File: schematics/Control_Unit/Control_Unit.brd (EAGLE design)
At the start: 49.8 x 49.8 mm, 222 parts, among them IC1 74HCT32N, IC10 74HC74N, IC100 74HCT374N, IC101 74HCT08N, IC102 74HC151N, IC103 74HC373N, IC105 74HC151N, IC106 74HC151N, IC108 74HCT32N, IC11 74HC74N, IC110 74HCT32N, IC111 74HC151N, IC112 74HCT32N, IC113 74HC151N, IC114 74HC151N, IC115 74HC151N, IC116 74HC373N, IC12 74AC08N, IC124 74HCT32N, IC125 74HCT08N, IC126 74AC157N, IC127 74HCT08N, IC128 74AC08N, IC129 74AC08N, IC13 74AC08N, IC135 74HCT08N, IC136 74HCT08N, IC14 74HC74N, IC141 74HCT32N, IC15 74HC74N, IC16 74AC08N, IC168 74HCT32N, IC17 74HCT32N, IC173 74HCT32N, IC175 74HC193N, IC176 74HC193N, IC177 74HC193N, IC178 74HC193N, IC179 74HC193N, IC18 74AC08N, IC180 74HC193N, IC181 74HC193N, IC182 74HC193N, IC19 74AC08N, IC191 74HCT32N, IC2 74HCT32N, IC20 74AC08N, IC21 74AC08N, IC22 74HCT32N, IC23 74HCT08N, IC24 74HCT08N, IC25 74HCT32N, IC26 74HCT08N, IC27 74HCT08N, IC28 74HCT08N, IC3 74HC151N, IC30 74HCT08N, IC31 74HCT00N, IC34 74HCT08N, IC35 74HCT04N, IC36 74HCT32N, IC39 74HCT08N, IC4 74AC08N, IC41 74HCT08N, IC42 74HC373N, IC43 74HCT04N, IC44 74ACT157N, IC46 74ACT157N, IC47 74HCT04N, IC48 74ACT02N, IC49 74AC86N, IC5 74ACT02N, IC51 74HCT08N, IC52 74HCT32N, IC55 74HCT32N, IC56 74HC151N, IC57 74HC151N, IC58 74HC151N, IC59 74HC151N, IC6 74HC193N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

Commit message: renumber schematic parts
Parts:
- removed C117, C120, C121, C122, C123, C127, C142, C143, C145, C148, C150, C151, C154: (no value), rcl:C1206
- removed IC110, IC112, IC124, IC168, IC173, IC191: 74HCT32N, 74xx-eu:DIL14
- removed IC113, IC114, IC115: 74HC151N, 74xx-eu:DIL16
- removed IC116: 74HC373N, 74xx-eu:DIL20
- removed IC125, IC127, IC135, IC136: 74HCT08N, 74xx-eu:DIL14
- removed IC126: 74AC157N, 74xx-eu:DIL16
- removed IC128, IC129: 74AC08N, 74xx-eu:DIL14
- removed IC175, IC176, IC177, IC179, IC180, IC181, IC182: 74HC193N, custom_parts:DIL16
- removed JP10: (no value), pinhead:2X20
- added C108, C24, C25, C37, C41, C45, C46, C54, C62, C66, C69, C76, C81: (no value), rcl:C1206
- added IC104: 74ACT157N, 74xx-eu:DIL16
- added IC107, IC62, IC76, IC92: 74HCT08N, 74xx-eu:DIL14
- added IC109: 74HCT00N, 74xx-eu:DIL14
- added IC29: 74ACT02N, 74xx-eu:DIL14
- added IC33, IC45, IC66, IC81: 74HCT374N, 74xx-eu:DIL20
- added IC37, IC38, IC50: 74HC151N, 74xx-eu:DIL16
- added IC40, IC68, IC94, IC96: 74HCT32N, 74xx-eu:DIL14
- added IC53, IC54: 74HC74N, 74xx-eu:DIL14
- added IC67: 74HCT04N, 74xx-eu:DIL14
- added IC69, IC75: 74HC193N, custom_parts:DIL16
- added IC95: 74AC08N, 74xx-eu:DIL14
- added JP4: (no value), pinhead:2X20
- IC10: value 74HC74N -> 74HCT08N
- IC100, IC99: value 74HCT374N -> 74HCT08N; device 74xx-eu:DIL20 -> 74xx-eu:DIL14
- IC101: value 74HCT08N -> 74HC373N; device 74xx-eu:DIL14 -> 74xx-eu:DIL20
- IC102, IC106, IC57, IC58, IC60: value 74HC151N -> 74HC193N; device 74xx-eu:DIL16 -> custom_parts:DIL16
- IC105, IC56, IC61: value 74HC151N -> 74HCT32N; device 74xx-eu:DIL16 -> 74xx-eu:DIL14
- IC108, IC2: value 74HCT32N -> 74HCT08N
- IC11: value 74HC74N -> 74ACT157N; device 74xx-eu:DIL14 -> 74xx-eu:DIL16
- IC12, IC13, IC21: value 74AC08N -> 74ACT157N; device 74xx-eu:DIL14 -> 74xx-eu:DIL16
- IC14: value 74HC74N -> 74HCT04N
- IC15: value 74HC74N -> 74HC151N; device 74xx-eu:DIL14 -> 74xx-eu:DIL16
- IC16, IC4: value 74AC08N -> 74HC151N; device 74xx-eu:DIL14 -> 74xx-eu:DIL16
- IC18: value 74AC08N -> 74HCT374N; device 74xx-eu:DIL14 -> 74xx-eu:DIL20
- IC19: value 74AC08N -> 74ACT02N
- IC20: value 74AC08N -> 74HCT08N
- IC22: value 74HCT32N -> 74HC151N; device 74xx-eu:DIL14 -> 74xx-eu:DIL16
- IC23, IC51: value 74HCT08N -> 74HC151N; device 74xx-eu:DIL14 -> 74xx-eu:DIL16
- IC25: value 74HCT32N -> 74AC86N
- IC26, IC41: value 74HCT08N -> 74HCT374N; device 74xx-eu:DIL14 -> 74xx-eu:DIL20
- IC27, IC34: value 74HCT08N -> 74ACT157N; device 74xx-eu:DIL14 -> 74xx-eu:DIL16
- IC28: value 74HCT08N -> 74AC08N
- IC31: value 74HCT00N -> 74HC151N; device 74xx-eu:DIL14 -> 74xx-eu:DIL16
- IC35: value 74HCT04N -> 74HC373N; device 74xx-eu:DIL14 -> 74xx-eu:DIL20
- IC36: value 74HCT32N -> 74HC373N; device 74xx-eu:DIL14 -> 74xx-eu:DIL20
- IC39: value 74HCT08N -> 74ACT02N
- IC42: value 74HC373N -> 74HC151N; device 74xx-eu:DIL20 -> 74xx-eu:DIL16
- IC43, IC47: value 74HCT04N -> 74HC151N; device 74xx-eu:DIL14 -> 74xx-eu:DIL16
- IC44: value 74ACT157N -> 74ACT02N; device 74xx-eu:DIL16 -> 74xx-eu:DIL14
- IC46: value 74ACT157N -> 74HC151N
- IC48, IC8: value 74ACT02N -> 74HCT32N
- IC49: value 74AC86N -> 74HCT32N
- IC5, IC85: value 74ACT02N -> 74HCT374N; device 74xx-eu:DIL14 -> 74xx-eu:DIL20
- IC52, IC55: value 74HCT32N -> 74HC74N
- IC59: value 74HC151N -> 74HCT08N; device 74xx-eu:DIL16 -> 74xx-eu:DIL14
- IC6, IC7, IC82, IC83: value 74HC193N -> 74AC08N; device custom_parts:DIL16 -> 74xx-eu:DIL14
- IC63, IC70, IC71, IC84: value 74HCT374N -> 74HCT32N; device 74xx-eu:DIL20 -> 74xx-eu:DIL14
- IC64, IC93: value 74HCT374N -> 74HC193N; device 74xx-eu:DIL20 -> custom_parts:DIL16
- IC72: value 74HC373N -> 74HCT08N; device 74xx-eu:DIL20 -> 74xx-eu:DIL14
- IC74: value 74HCT08N -> 74HC193N; device 74xx-eu:DIL14 -> custom_parts:DIL16
- IC77, IC87: value 74ACT157N -> 74AC08N; device 74xx-eu:DIL16 -> 74xx-eu:DIL14
- IC79: value 74ACT157N -> 74HCT374N; device 74xx-eu:DIL16 -> 74xx-eu:DIL20
- IC80: value 74HCT32N -> 74HC193N; device 74xx-eu:DIL14 -> custom_parts:DIL16
- IC86: value 74ACT157N -> 74HCT04N; device 74xx-eu:DIL16 -> 74xx-eu:DIL14
- IC88, IC89: value 74ACT157N -> 74HCT08N; device 74xx-eu:DIL16 -> 74xx-eu:DIL14
- IC9: value 74HC151N -> 74AC157N
- IC90, IC91: value 74HCT374N -> 74AC08N; device 74xx-eu:DIL20 -> 74xx-eu:DIL14
- IC98: value 74HC151N -> 74ACT157N
- JP1: device pinhead:2X20 -> pinhead:2X15
- JP3: device pinhead:2X15 -> pinhead:2X20
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- renumbered C110 to C107, C111 to C106, C112 to C103, C113 to C105, C114 to C104, C116 to C102, C118 to C101, C126 to C98, C129 to C100, C130 to C95, C131 to C97, C132 to C96, C141 to C94, C144 to C92, C146 to C89, C147 to C88, C153 to C83, IC111 to IC32, IC141 to IC65, IC178 to IC97, JP9 to JP5
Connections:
- net !CLR_CARRY_BIT: now also IC55.13, JP4.12; no longer IC15.13, JP1.12
- net !IR_DATA_OUT_7: now also IC40.12, IC59.10, IC86.10, IC88.12; no longer IC101.12, IC127.10, IC36.12, IC47.10
- net !OPCODE_5: now also IC14.6, IC28.2, IC28.5, IC92.10; no longer IC129.2, IC129.5, IC26.10, IC43.6
- net !REGISTER_RESET: now also IC102.14, IC106.14, IC57.14, IC58.14, IC60.14, IC64.14, IC69.14, IC74.14, IC75.14, IC80.14, IC93.14, JP4.8; no longer IC175.14, IC176.14, IC177.14, IC179.14, IC180.14, IC181.14, IC182.14, IC6.14, IC7.14, IC82.14, IC83.14, JP1.8
- net !RING_CNTR_RESET: now also IC52.13, IC52.4, IC53.1, IC53.13, IC54.1, IC54.13, IC55.1, JP4.10; no longer IC10.13, IC10.4, IC11.1, IC11.13, IC14.1, IC14.13, IC15.1, JP1.10
- net !SET_CARRY_BIT: now also IC55.10, JP4.14; no longer IC15.10, JP1.14
- net !TWO_BYTE_CMD: now also IC14.11, IC89.10, IC96.8; no longer IC108.8, IC23.10, IC43.11
- net ADRR_0: now also IC13.4, JP1.1; no longer IC86.4, JP2.1
- net ADRR_1: now also IC13.7, JP1.3; no longer IC86.7, JP2.3
- net ADRR_10: now also IC27.9, JP1.21; no longer IC88.9, JP2.21
- net ADRR_11: now also IC27.12, JP1.23; no longer IC88.12, JP2.23
- net ADRR_12: now also IC34.4, JP1.25; no longer IC89.4, JP2.25
- net ADRR_13: now also IC34.7, JP1.27; no longer IC89.7, JP2.27
- net ADRR_14: now also IC34.9, JP1.29; no longer IC89.9, JP2.29
- net ADRR_15: now also IC34.12, IC67.5, IC68.9; no longer IC17.9, IC35.5, IC89.12
- net ADRR_2: now also IC13.9, JP1.5; no longer IC86.9, JP2.5
- net ADRR_3: now also IC13.12, JP1.7; no longer IC86.12, JP2.7
- net ADRR_4: now also IC21.4, JP1.9; no longer IC87.4, JP2.9
- net ADRR_5: now also IC21.7, JP1.11; no longer IC87.7, JP2.11
- net ADRR_6: now also IC21.9, JP1.13; no longer IC87.9, JP2.13
- net ADRR_7: now also IC21.12, JP1.15; no longer IC87.12, JP2.15
- net ADRR_8: now also IC27.4, JP1.17; no longer IC88.4, JP2.17
- net ADRR_9: now also IC27.7, JP1.19; no longer IC88.7, JP2.19
- net ALU_CARRY_BIT: now also IC55.9, IC62.4, JP4.16; no longer IC15.9, IC34.4, JP1.16
- net ALU_CARRY_IN: now also IC62.6; no longer IC34.6
- net ALU_CARRY_OUT: now also IC109.12, IC55.12, IC88.9; no longer IC101.9, IC15.12, IC31.12
- net ALU_NR1_ENABLE_ALU: now also IC49.9, IC70.1, IC77.3; no longer IC18.3, IC191.1, IC25.9
- net ALU_NR1_ENABLE_JMP_O_PTR_ADD: now also IC49.10, IC59.8; no longer IC127.8, IC25.10
- net ALU_NR2_ENABLE_ALU: now also IC49.12, IC70.2, IC77.6; no longer IC18.6, IC191.2, IC25.12
- net ALU_NR2_ENABLE_JMP_O_PTR_ADD: now also IC108.8, IC49.13; no longer IC125.8, IC25.13
- net ALU_NR3_ENABLE_ALU: now also IC70.4, IC77.8; no longer IC18.8, IC191.4
- net ALU_NR4_ENABLE_ALU: now also IC70.5, IC77.11; no longer IC18.11, IC191.5
- net CLR_NOT_CS/FILL_REGISTER_LDR: now also IC105.1, IC107.8, IC68.4, IC96.5; no longer IC108.5, IC17.4, IC173.1, IC27.8
- net CLR_NOT_CS_POP/FILL_REGISTER_POP: now also IC108.3, IC19.9, IC39.11, IC96.4; no longer IC108.4, IC125.3, IC48.11, IC85.9
- net CLR_NOT_CS_PUSH: now also IC105.4, IC107.3, IC19.8; no longer IC173.4, IC27.3, IC85.8
- net CLR_NOT_CS_STR: now also IC105.9, IC107.11, IC68.2; no longer IC17.2, IC173.9, IC27.11
- net CLR_NOT_OE/CLR_NOT_CS_CYCL_1/2: now also IC19.11, IC68.1, IC84.6; no longer IC17.1, IC80.6, IC85.11
- net CLR_NOT_OE/CLR_NOT_CS_CYCL_3/4: now also IC68.5, IC84.11; no longer IC17.5, IC80.11
- net CLR_NOT_OE_POP: now also IC39.13, JP2.4; no longer IC48.13, JP3.4
- net CNNCT_PTR_TO_ABUS/CNNCT_REG_TO_DBUS/CLR_NOT_WE/SEL_2_STR: now also IC105.8, IC17.9, IC40.2, IC67.3; no longer IC173.8, IC2.9, IC35.3, IC36.2
- net CONNECT_PTR_TO_ABUS/CLR_NOT_OE_LDR: now also IC105.3, IC19.12, IC40.1; no longer IC173.3, IC36.1, IC85.12
- net CONNECT_REG_TO_DBUS/CLR_NOT_WE/SELECTOR_TABLE_2_PUSH: now also IC105.6, IC17.10, IC67.1; no longer IC173.6, IC2.10, IC35.1
- net CONNECT_REG_TO_DBUS_PTR/FILL_PTR_L_SET_PTR: now also IC39.3, IC61.4, IC99.11; no longer IC24.11, IC48.3, IC52.4
- net CYCL_1: now also IC52.12, IC52.5, IC84.5, JP4.22; no longer IC10.12, IC10.5, IC80.5, JP1.22
- net DATA0: now also IC101.2, IC18.3, IC26.3, IC33.3, IC35.2, IC36.2, IC41.3, IC45.3, IC5.3, IC57.15, IC60.15, IC66.3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; no longer IC100.3, IC116.2, IC179.15, IC181.15, IC42.2, IC63.3, IC64.3, IC70.3, IC71.3, IC72.2, IC77.2, IC82.15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
- net DATA1: now also IC101.5, IC18.4, IC26.4, IC33.4, IC35.5, IC36.5, IC41.4, IC45.4, IC5.4, IC57.1, IC60.1, IC66.4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; no longer IC100.4, IC116.5, IC179.1, IC181.1, IC42.5, IC63.4, IC64.4, IC70.4, IC71.4, IC72.5, IC77.5, IC82.1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
- net DATA2: now also IC101.6, IC18.7, IC26.7, IC33.7, IC35.6, IC36.6, IC41.7, IC45.7, IC5.7, IC57.10, IC60.10, IC66.7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; no longer IC100.7, IC116.6, IC179.10, IC181.10, IC42.6, IC63.7, IC64.7, IC70.7, IC71.7, IC72.6, IC77.11, IC82.10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
- net DATA3: now also IC101.9, IC18.8, IC26.8, IC33.8, IC35.9, IC36.9, IC41.8, IC45.8, IC5.8, IC57.9, IC60.9, IC66.8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; no longer IC100.8, IC116.9, IC179.9, IC181.9, IC42.9, IC63.8, IC64.8, IC70.8, IC71.8, IC72.9, IC77.14, IC82.9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
- net DATA4: now also IC101.12, IC104.2, IC18.13, IC26.13, IC33.13, IC35.12, IC36.12, IC41.13, IC45.13, IC5.13, IC58.15, IC64.15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; no longer IC100.13, IC116.12, IC180.15, IC182.15, IC42.12, IC63.13, IC64.13, IC70.13, IC71.13, IC72.12, IC79.2, IC83.15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
- net DATA5: now also IC101.15, IC104.5, IC18.14, IC26.14, IC33.14, IC35.15, IC36.15, IC41.14, IC45.14, IC5.14, IC58.1, IC64.1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; no longer IC100.14, IC116.15, IC180.1, IC182.1, IC42.15, IC63.14, IC70.14, IC71.14, IC72.15, IC79.5, IC83.1, IC84.14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
- net DATA6: now also IC101.16, IC104.11, IC18.17, IC26.17, IC33.17, IC35.16, IC36.16, IC41.17, IC45.17, IC5.17, IC58.10, IC64.10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; no longer IC100.17, IC116.16, IC180.10, IC182.10, IC42.16, IC63.17, IC64.14, IC64.17, IC70.17, IC71.17, IC72.16, IC79.11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
- net DATA7: now also IC101.19, IC104.14, IC18.18, IC26.18, IC33.18, IC35.19, IC36.19, IC41.18, IC45.18, IC5.18, IC58.9, IC64.9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; no longer IC100.18, IC116.19, IC180.9, IC182.9, IC42.19, IC63.18, IC64.18, IC70.18, IC71.18, IC72.19, IC79.14, IC83.9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
- net DATA_BUS_ENABLE_LATCH: now also IC35.11, IC59.3, IC67.9; no longer IC127.3, IC35.9, IC72.11
- net DBUS_SELECTOR_TABLE_2: now also IC11.1, IC17.8, IC63.1; no longer IC110.1, IC2.8, IC46.1
- net FDSGDFGFDSGFSDGFDGSDG: now also IC19.1, IC8.10, IC8.13; no longer IC22.10, IC22.13, IC85.1
- net FSDFAFSDFSFDDDDDDDDDDDDDDDDDDDDDDDDDDDDDDDD1: now also IC10.10, IC10.2, IC2.10, IC2.2, IC20.6; no longer IC136.6, IC39.10, IC39.2, IC41.10, IC41.2
- net GND: now also C108.2, C24.2, C25.2, C37.2, C41.2, C45.2, C46.2, C54.2, C62.2, C66.2, C69.2, C76.2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; no longer C117.2, C120.2, C121.2, C122.2, C123.2, C127.2, C142.2, C143.2, C145.2, C148.2, C150.2, C151.2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
- net HGGJHGGJZGZ77UZGHGHHGHGHGHGHJGHJ: now also IC100.8, IC105.2; no longer IC173.2, IC51.8
- net INPUT_REG0/OPC4/5_IS_NULL: now also IC109.5, IC2.1, IC2.4, IC24.1, IC24.4, IC28.3, IC88.1, IC9.3; no longer IC101.1, IC126.3, IC129.3, IC135.1, IC135.4, IC31.5, IC41.1, IC41.4
- net INPUT_REG1: now also IC2.12, IC2.9, IC24.12, IC24.9, IC28.6, IC9.6; no longer IC126.6, IC129.6, IC135.12, IC135.9, IC41.12, IC41.9
- net INPUT_REG2: now also IC10.1, IC10.4, IC28.8, IC9.10; no longer IC126.10, IC129.8, IC39.1, IC39.4
- net INPUT_REG3: now also IC10.12, IC10.9, IC28.11, IC9.13; no longer IC126.13, IC129.11, IC39.12, IC39.9
- net INPUT_REG_IS_NOT_OUTPUT_REG: now also IC17.6, IC19.3, IC6.1, IC6.12, IC6.4, IC6.9, IC96.9; no longer IC108.9, IC2.6, IC4.1, IC4.12, IC4.4, IC4.9, IC85.3
- net IO_INPUT1_0: now also IC3.12, JP3.2; no longer IC61.12, JP10.2
- net IO_INPUT1_1: now also IC15.12, JP3.4; no longer IC60.12, JP10.4
- net IO_INPUT1_2: now also IC22.12, JP3.6; no longer IC59.12, JP10.6
- net IO_INPUT1_3: now also IC31.12, JP3.8; no longer IC58.12, JP10.8
- net IO_INPUT1_4: now also IC37.12, JP3.10; no longer IC57.12, JP10.10
- net IO_INPUT1_5: now also IC42.12, JP3.12; no longer IC56.12, JP10.12
- net IO_INPUT1_6: now also IC46.12, JP3.14; no longer IC3.12, JP10.14
- net IO_INPUT1_7: now also IC50.12, JP3.16; no longer IC9.12, JP10.16
- net IO_INPUT2_0: now also IC4.15, JP3.24; no longer IC115.15, JP10.24
- net IO_INPUT2_1: now also IC16.15, JP3.26; no longer IC114.15, JP10.26
- net IO_INPUT2_2: now also IC23.15, JP3.28; no longer IC113.15, JP10.28
- net IO_INPUT2_3: now also JP3.30; no longer JP10.30
- net IO_INPUT2_4: now also IC38.15, JP3.32; no longer IC106.15, JP10.32
- net IO_INPUT2_5: now also IC43.15, JP3.34; no longer IC105.15, JP10.34
- net IO_INPUT2_6: now also IC47.15, JP3.36; no longer IC98.15, JP10.36
- net IO_INPUT2_7: now also IC51.15, JP3.38; no longer IC102.15, JP10.38
- net IO_OUTPUT1_0: now also IC4.14, IC73.2, JP3.1; no longer IC115.14, IC63.2, JP10.1
- net IO_OUTPUT1_1: now also IC16.14, IC73.5, JP3.3; no longer IC114.14, IC63.5, JP10.3
- net IO_OUTPUT1_2: now also IC23.14, IC73.6, JP3.5; no longer IC113.14, IC63.6, JP10.5
- net IO_OUTPUT1_3: now also IC73.9, JP3.7; no longer IC63.9, JP10.7
- net IO_OUTPUT1_4: now also IC38.14, IC73.12, JP3.9; no longer IC106.14, IC63.12, JP10.9
- net IO_OUTPUT1_5: now also IC43.14, IC73.15, JP3.11; no longer IC105.14, IC63.15, JP10.11
- net IO_OUTPUT1_6: now also IC47.14, IC73.16, JP3.13; no longer IC63.16, IC98.14, JP10.13
- net IO_OUTPUT1_7: now also IC51.14, IC73.19, JP3.15; no longer IC102.14, IC63.19, JP10.15
- net IO_OUTPUT2_0: now also IC4.13, IC79.2, JP3.23; no longer IC115.13, IC64.2, JP10.23
- net IO_OUTPUT2_1: now also IC16.13, IC79.5, JP3.25; no longer IC114.13, IC64.5, JP10.25
- net IO_OUTPUT2_2: now also IC23.13, IC79.6, JP3.27; no longer IC113.13, IC64.6, JP10.27
- net IO_OUTPUT2_3: now also IC79.9, JP3.29; no longer IC64.9, JP10.29
- net IO_OUTPUT2_4: now also IC38.13, IC79.12, JP3.31; no longer IC106.13, IC64.12, JP10.31
- net IO_OUTPUT2_5: now also IC43.13, IC79.15, JP3.33; no longer IC105.13, IC64.15, JP10.33
- net IO_OUTPUT2_6: now also IC47.13, IC79.16, JP3.35; no longer IC64.16, IC98.13, JP10.35
- net IO_OUTPUT2_7: now also IC51.13, IC79.19, JP3.37; no longer IC102.13, IC64.19, JP10.37
- net IO_OUTPUT_REG_1_LOAD_INPUT: now also IC10.8, IC73.11; no longer IC39.8, IC63.11
- net IO_OUTPUT_REG_2_LOAD_INPUT: now also IC10.11, IC79.11; no longer IC39.11, IC64.11
- net IR_DATA_OUT_0: now also IC3.4, IC41.2; no longer IC61.4, IC90.2
- net IR_DATA_OUT_1: now also IC15.4, IC41.5; no longer IC60.4, IC90.5
- net IR_DATA_OUT_2: now also IC22.4, IC41.6; no longer IC59.4, IC90.6
- net IR_DATA_OUT_3: now also IC31.4, IC41.9; no longer IC58.4, IC90.9
- net IR_DATA_OUT_4: now also IC37.4, IC41.12; no longer IC57.4, IC90.12
- net IR_DATA_OUT_5: now also IC41.15, IC42.4; no longer IC56.4, IC90.15
- net IR_DATA_OUT_6: now also IC41.16, IC46.4; no longer IC3.4, IC90.16
- net IR_DATA_OUT_7: now also IC108.10, IC40.9, IC41.19, IC50.4, IC86.11, IC88.4; no longer IC101.4, IC125.10, IC36.9, IC47.11, IC9.4, IC90.19
- net IR_LOAD_INPUT/PC_COUNT_UP_FETCH2/CYCL_4: now also IC41.11, IC49.1, IC53.9, IC56.2, IC84.12, JP4.28; no longer IC1.2, IC11.9, IC25.1, IC80.12, IC90.11, JP1.28
- net LATCH_ALU_INPUT_B_ALU: now also IC63.12, IC71.1, IC72.3; no longer IC110.12, IC124.1, IC28.3
- net LATCH_ALU_INPUT_B_JMP_O: now also IC63.9, IC84.1; no longer IC110.9, IC80.1
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
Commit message: fix WRITE_TO_DBUS signal
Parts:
- removed IC62: 74HCT08N, 74xx-eu:DIL14
- added IC112: 74HCT32N, 74xx-eu:DIL14
- added IC118, IC131: 74HC74N, 74xx-eu:DIL14
- added IC126, IC130: 74HCT08N, 74xx-eu:DIL14
- IC105: value 74HCT32N -> 74HC74N
- IC129: value 74HCT32N -> 74HCT04N
- IC52: value 74HC74N -> 74HCT08N
- IC55: value 74HC74N -> 74HCT32N
- moved IC55 52.7 mm to (61.9, 31.1)
- moved IC105 44.8 mm to (30.5, 44.8)
- moved IC52 27.0 mm to (3.17, 9.21)
- renumbered IC107 to IC125, IC63 to IC129
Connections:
- net N$32 renamed REG_TO_DBUS_L_JMP_RET
- net N$33 renamed REG_TO_DBUS_H_JMP_RET
- removed net CLR_NOT_CS/FILL_REGISTER_LDR: IC105.1, IC125.8, IC68.4, IC96.5
- removed net CLR_NOT_CS_POP/FILL_REGISTER_POP: IC108.3, IC19.9, IC39.11, IC96.4
- removed net CLR_NOT_CS_PUSH: IC105.4, IC125.3, IC19.8
- removed net CLR_NOT_CS_STR: IC105.9, IC125.11, IC68.2
- removed net CLR_NOT_OE/CLR_NOT_CS_CYCL_1/2: IC19.11, IC68.1, IC84.6
- removed net CLR_NOT_OE/CLR_NOT_CS_CYCL_3/4: IC68.5, IC84.11
- removed net CLR_NOT_OE_POP: IC39.13, JP2.4
- removed net CNNCT_PTR_TO_ABUS/CNNCT_REG_TO_DBUS/CLR_NOT_WE/SEL_2_STR: IC105.8, IC17.9, IC40.2, IC67.3
- removed net CONNECT_PTR_TO_ABUS/CLR_NOT_OE_LDR: IC105.3, IC19.12, IC40.1
- removed net CONNECT_REG_TO_DBUS/CLR_NOT_WE/SELECTOR_TABLE_2_PUSH: IC105.6, IC17.10, IC67.1
- removed net CONNECT_REG_TO_DBUS_PTR/FILL_PTR_L_SET_PTR: IC39.3, IC61.4, IC99.11
- removed net CYCL_1: IC52.12, IC52.5, IC84.5, JP4.22
- removed net HGGJHGGJZGZ77UZGHGHHGHGHGHGHJGHJ: IC100.8, IC105.2
- removed net IR_LOAD_INPUT/PC_COUNT_UP_FETCH2/CYCL_4: IC41.11, IC49.1, IC53.9, IC56.2, IC84.12, JP4.28
- removed net LATCH_ALU_INPUT_B_ALU: IC129.12, IC71.1, IC72.3
- removed net LATCH_ALU_INPUT_B_JMP_O: IC129.9, IC78.11, IC84.1
- removed net LATCH_ALU_INPUT_B_PTR_ADD: IC105.12, IC129.10, IC89.3
- removed net N$109: IC76.11, IC84.2
- removed net N$110: IC71.2, IC76.6
- removed net N$123: IC100.11, IC105.10
- removed net N$132: IC108.6, IC71.4, IC72.13, IC76.13, IC78.13
- removed net N$146: IC105.5, IC125.6
- removed net N$151: IC105.13, IC99.6
- removed net N$152: IC129.13, IC129.8
- removed net N$157: IC100.6, IC39.12
- removed net OPCODE_LOAD_INPUT/CYCL_2: IC45.11, IC52.9, IC53.2, IC84.4, JP4.24
- removed net PC_COUNT_UP_FETCH1/CYCL_3: IC53.12, IC56.1, IC84.13, IC89.11, JP4.26
- removed net PTR_ADD_OR_JMP_O_OR_ALU_FILL: IC1.4, IC1.8, IC14.9
- removed net STATE_0/CYCL_5: IC100.12, IC100.4, IC100.9, IC109.9, IC54.12, IC54.5, IC76.1, IC76.12, IC76.4, IC76.9, IC99.1, IC99.12, IC99.4, IC99.9, JP4.30
- removed net STATE_1/CYCL_6: IC100.1, IC108.1, IC125.12, IC125.4, IC125.9, IC54.9, IC55.2, IC72.1, IC72.9, IC78.12, IC89.1, IC92.1, IC92.4, JP4.32
- removed net STATE_2/CYCL_7: IC109.1, IC125.1, IC52.2, IC55.5, IC72.12, IC72.4, IC89.4, JP4.34
- removed net WRITE_LR_H_DBUS/FILL_PC_H_RET: IC100.3, IC40.4, IC56.4, IC65.2
- removed net WRITE_LR_L_DBUS_RET/FILL_PC_L_RET: IC56.10, IC65.1, IC99.3
- removed net WRITE_PC_H_DBUS/FILL_LR_H_SAVE_LR: IC44.11, IC65.13, IC92.6
- removed net WRITE_PC_L_DBUS/FILL_LR_L_SAVE_LR: IC40.5, IC44.8, IC65.12, IC99.8
- removed net WRITE_REGB_TO_DBUS/FILL_PC_L_JMP_O: IC1.2, IC56.12, IC72.11, IC88.10
- removed net WRITE_REGB_TO_DBUS/FILL_PTR_H_SET_PTR: IC1.13, IC39.6, IC92.3
- removed net WRITE_REGB_TO_DBUS/FILL_PTR_L_PTR_ADD: IC1.1, IC109.13, IC72.6
- removed net WRITE_REGB_TO_DBUS/FILL_REGISTER/ALU_TO_DBUS_ALU: IC1.10, IC17.13, IC55.11, IC89.6
- removed net WRITE_REGB_TO_DBUS/PC_HIGH_LOAD_INPUT_JMP: IC1.12, IC44.5, IC72.8
- removed net WRITE_REG_TO_DBUS_JMP/PC_LOW_LOAD_INPUT_JMP: IC56.9, IC61.1, IC76.8
- removed net WRITE_REG_TO_DBUS_MOV/FILL_REGISTER_MOV: IC17.12, IC61.5, IC76.3
- new net !ENABLE_REG_OUTPUT: IC112.1, IC55.11, IC84.5
- new net ALU_OUTPUT_ENABLE/FILL_PC_L_JMP_O: IC112.5, IC56.12, IC72.11, IC88.10
- new net ALU_OUTPUT_ENABLE/FILL_PTR_L_PTR_ADD: IC1.1, IC109.13, IC55.2, IC72.6
- new net CARRY_LAST_CYCLE: IC109.12, IC118.9, IC88.9
- new net CLR_NOT_OE/CLR_NOT_CS_CYCL_1: IC19.11, IC53.5, IC55.5, IC68.1, IC89.12, IC89.9, JP4.26
- new net CLR_NOT_OE/CLR_NOT_CS_CYCL_2: IC49.1, IC53.9, IC55.4, IC68.5, JP4.28
- new net CLR_NOT_OE/CLR_NOT_CS_POP/FILL_REGISTER_POP: IC100.6, IC19.9, IC96.4, JP2.4
- new net ENABLE_ALU_OUTPUT: IC14.9, IC55.10, IC55.3
- new net ENABLE_ALU_OUTPUT/FILL_REGISTER_ALU: IC112.4, IC17.13, IC52.6
- new net IR_LOAD_INPUT/PC_COUNT_UP/!CYCL_2: IC41.11, IC49.5, IC53.8
- new net LATCH_ALU_INPUT_B/WRITE_REGB_TO_DBUS_JMP_O: IC1.2, IC76.11, IC84.12
- new net N$18: IC53.12, IC89.11
- new net N$32: IC55.13, IC55.8
- new net N$33: IC55.12, IC55.6
- new net N$74: IC118.3, IC129.2
- new net N$79: IC112.12, IC112.8
- new net N$81: IC129.11, IC129.8
- new net N$83: IC129.10, IC129.13
- new net N$84: IC129.12, IC130.2
- new net N$85: IC131.9, IC84.4
- new net N$86: IC112.6, IC55.1
- new net N$87: IC130.3, IC131.11
- new net N$88: IC112.2, IC131.8
- new net N$89: IC101.1, IC14.8
- new net N$91: IC1.4, IC1.8
- new net OPCODE_LOAD_INPUT/PC_COUNT_UP/!CYCL_1: IC45.11, IC49.4, IC53.6
- new net REG_TO_DBUS_B_ALU_PTR_ADD: IC84.13, IC84.3
- new net REG_TO_DBUS_ENABLE/CLR_NOT_CS/CLR_NOT_WE_PUSH: IC126.6, IC19.8, IC67.1
- new net REG_TO_DBUS_ENABLE/FILL_LR_H_SAVE_LR: IC125.6, IC44.11
- new net REG_TO_DBUS_ENABLE/FILL_LR_L_SAVE_LR: IC44.8, IC92.6
- new net REG_TO_DBUS_ENABLE/FILL_PC_H_RET: IC126.8, IC56.4
- new net REG_TO_DBUS_ENABLE/FILL_PC_L_RET: IC100.3, IC56.10
- new net REG_TO_DBUS_ENABLE/FILL_PTR_H_SET_PTR: IC125.11, IC39.6
- new net REG_TO_DBUS_ENABLE/FILL_PTR_L_SET_PTR: IC39.3, IC92.3
- new net REG_TO_DBUS_ENABLE/FILL_REGISTER_MOV: IC108.3, IC17.12
- new net REG_TO_DBUS_ENABLE/LATCH_ALU_INPUT_B/WRITE_REGB_TO_DBUS_ALU: IC1.10, IC72.3, IC84.1
- new net REG_TO_DBUS_ENABLE/LATCH_ALU_INPUT_B/WRITE_REGB_TO_DBUS_PTR_ADD: IC84.2, IC89.3
- new net REG_TO_DBUS_ENABLE/PC_HIGH_LOAD_INPUT_JMP: IC52.8, IC56.5
- new net REG_TO_DBUS_ENABLE/PC_LOW_LOAD_INPUT_JMP: IC56.9, IC72.8
- new net REG_TO_DBUS_ENABLE/STORE_ALU_OUTPUT/STORE_CARRY_ALU: IC112.9, IC129.1, IC52.3
- new net REG_TO_DBUS_ENABLE/STORE_ALU_OUTPUT/STORE_CARRY_TMP_JMP_O: IC112.10, IC39.11, IC78.11
- new net REG_TO_DBUS_ENABLE/STORE_ALU_OUTPUT/STORE_CARRY_TMP_PTR_ADD: IC112.13, IC125.3, IC39.12
- new net REG_TO_DBUS_ENABLE/WRITE_PTR_TO_ABUS/CLR_NOT_WE/CLR_NOT_CS_STR: IC130.8, IC40.2, IC67.3, IC68.2
- new net STATE_0/CYCL_3: IC100.12, IC100.4, IC100.9, IC130.4, IC54.12, IC54.5, IC76.1, IC76.12, IC76.4, IC76.9, IC99.1, IC99.12, IC99.4, IC99.9, JP4.30
- new net STATE_1/CYCL_4: IC100.1, IC105.2, IC108.1, IC109.1, IC126.4, IC130.9, IC54.9, IC72.1, IC72.9, IC78.12, IC89.1, IC92.1, IC92.4, JP4.32
- new net STATE_2/CYCL_5: IC105.12, IC105.5, IC125.1, IC125.9, IC126.1, IC126.12, IC52.1, IC52.12, IC72.12, JP4.34
- new net STATE_3/CYCL_6: IC105.9, IC125.12, IC125.4, IC126.9, IC52.4, IC52.9, IC53.2, IC72.4
- new net STORE_ALU_OUTPUT: IC101.11, IC112.11
- new net WRITE_LR_H_DBUS_RET: IC126.3, IC40.4, IC65.2
- new net WRITE_LR_L_DBUS_RET: IC65.1, IC99.3
- new net WRITE_PC_H_DBUS_SAVE_LR: IC126.11, IC65.13
- new net WRITE_PC_L_DBUS_SAVE_LR: IC40.5, IC65.12, IC99.8
- new net WRITE_PTR_TO_ABUS/CLR_NOT_OE/CLR_NOT_CS/FILL_REGISTER_LDR: IC100.8, IC19.12, IC40.1, IC55.9, IC68.4, IC96.5
- new net WRITE_REGB_TO_DBUS_JMP: IC1.12, IC52.11
- new net WRITE_REGB_TO_DBUS_SET_PTR: IC1.13, IC125.8
- new net WRITE_REG_TO_DBUS_JMP: IC61.1, IC76.8
- new net WRITE_REG_TO_DBUS_MOV: IC61.5, IC76.3
- new net WRITE_REG_TO_DBUS_SELECTOR2_PUSH: IC130.6, IC17.10, IC67.9
- new net WRITE_REG_TO_DBUS_SELECTOR2_STR: IC100.11, IC17.9
- new net WRITE_REG_TO_DBUS_SET_PTR: IC61.4, IC99.11
- net !CLR_CARRY_BIT: now also IC118.1; no longer IC55.13
- net !RING_CNTR_RESET: now also IC105.1, IC105.13, IC53.4; no longer IC52.13, IC52.4, IC53.1, IC55.1
- net !SET_CARRY_BIT: now also IC118.4; no longer IC55.10
- net ALU_CARRY_BIT: now also IC118.5, IC89.4; no longer IC55.9, IC62.4
- net ALU_CARRY_IN: now also IC89.6; no longer IC62.6
- net ALU_CARRY_OUT: now also IC118.12, IC118.2; no longer IC109.12, IC55.12, IC88.9
- net DATA_BUS_ENABLE_LATCH: no longer IC67.9
- net DBUS_SELECTOR_TABLE_2: now also IC56.1; no longer IC129.1
- net GND: now also IC112.7, IC118.7, IC126.7, IC130.7, IC131.7, JP4.22, JP4.24; no longer IC62.7
- net LDR: no longer IC125.10
- net N$12: no longer IC67.11
- net N$14: now also IC118.11, IC39.13; no longer IC101.1, IC101.11, IC14.8
- net N$15: now also IC52.10, IC52.13
- net N$190: now also IC94.2; no longer IC96.2
- net N$192: now also IC94.1, IC96.3; no longer IC94.3, IC96.1
- net N$193: now also IC94.3; no longer IC96.3
- net N$194: now also IC125.5, IC126.13
- net N$2: now also IC56.3, IC71.1; no longer IC129.3, IC129.4
- net N$219: now also IC126.10, IC126.2
- net N$266: now also IC129.5
- net N$44: now also IC112.3, IC36.1; no longer IC53.5, IC89.12, IC89.9
- net N$52: now also IC129.6, IC129.9, IC130.1; no longer IC36.1, IC67.10
- net N$55: now also IC108.2
- net N$7: now also IC129.4; no longer IC67.12
- net N$90: now also IC71.3; no longer IC129.6
- net N$96: now also IC84.11; no longer IC129.11
- net N$97: now also IC125.10, IC125.13
- net OPERAND_REGB_OUTPUT: now also IC56.2; no longer IC129.2
- net PC_COUNT_UP: now also IC49.6; no longer IC56.3
- net PC_H_LOAD_INPUT_TABLE_1: now also IC44.5; no longer IC56.5
- net POP: no longer IC108.2
- net PTR_ADD: now also IC125.2
- net PUSH: now also IC126.5, IC130.5; no longer IC109.10, IC125.2, IC125.5
- net REGISTER_OUTPUT_SEL_3: now also IC129.3, IC131.12; no longer IC67.13
- net REGS_OUTPUT_TO_DATABUS_ENABLE: now also IC84.6; no longer IC67.8
- net REG_0_OUT_0: now also IC96.1; no longer IC94.1
- net REG_0_OUT_1: now also IC96.2; no longer IC94.2
- net RING_CNTR_CLOCK: now also IC105.11, IC105.3; no longer IC52.11, IC52.3, IC55.3
- net SELECT_CARRY_BIT: now also IC52.2, IC52.5; no longer IC62.5
- net SP_COUNT_UP: now also IC67.8; no longer IC109.8
- net STR: now also IC130.10; no longer IC125.13
- net VCC: now also IC105.10, IC105.4, IC112.14, IC118.10, IC118.13, IC118.14, IC126.14, IC130.14, IC131.10, IC131.13, IC131.14, IC53.1; no longer IC52.1, IC52.10, IC53.4, IC55.4, IC62.14
- net WRITE_PC_L_ALU_LATCH_JMP_O: now also IC108.6, IC71.4, IC72.13, IC76.13, IC78.13; no longer IC84.3
- net WRITE_PTR_L_TO_DBUS_PTR_ADD: now also IC71.2, IC99.6; no longer IC105.11, IC129.5
- net WRITE_REG_TO_DBUS_ALU: now also IC76.6; no longer IC71.3

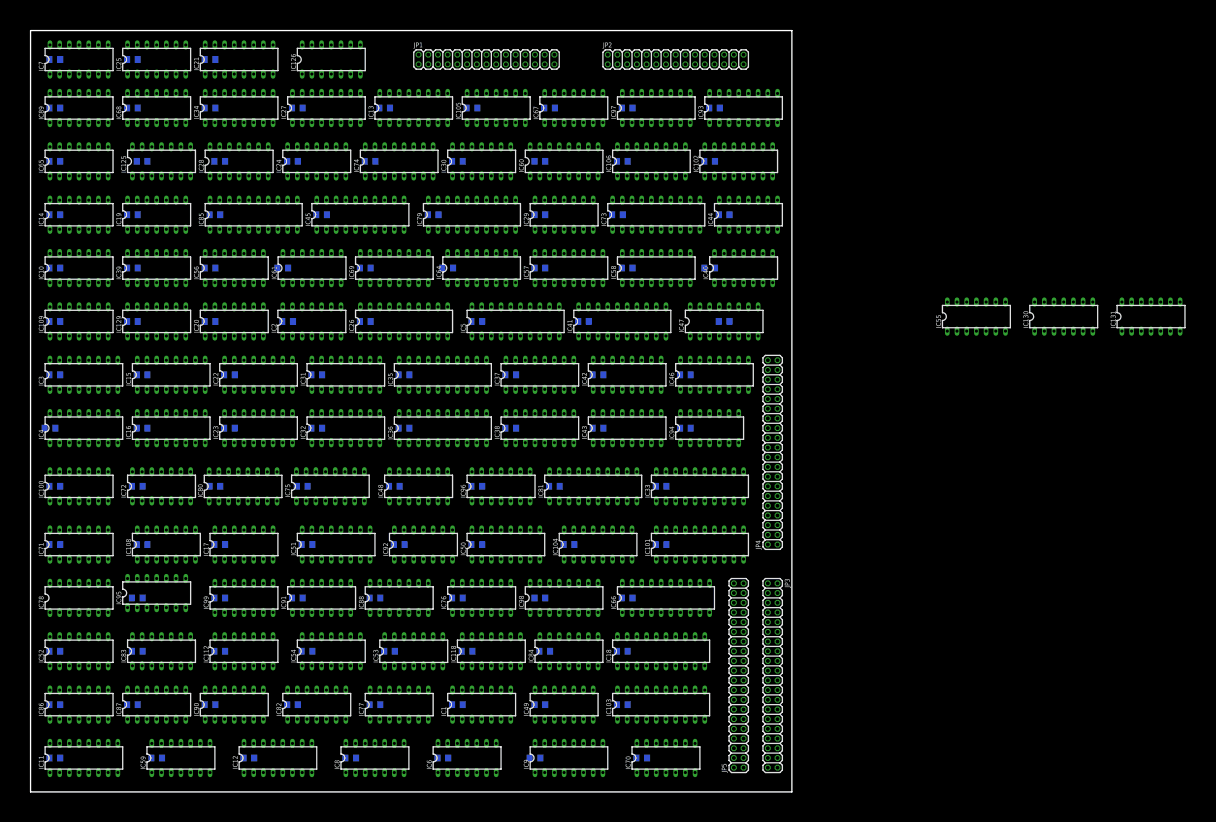
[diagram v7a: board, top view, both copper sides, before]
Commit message: optimize part count
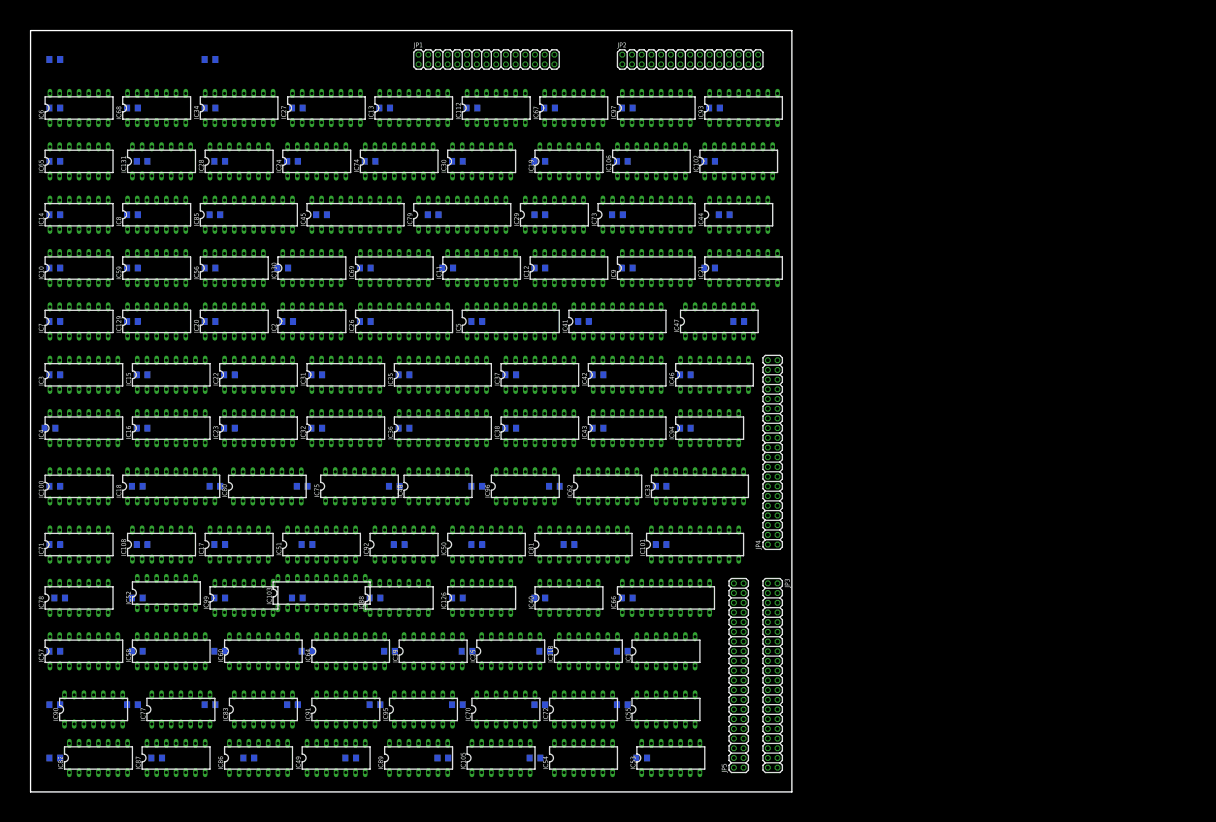
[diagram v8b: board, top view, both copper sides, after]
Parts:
- removed IC104, IC98: 74ACT157N, 74xx-eu:DIL16
- removed IC109: 74HCT00N, 74xx-eu:DIL14
- removed IC125, IC76: 74HCT08N, 74xx-eu:DIL14
- removed IC61, IC84: 74HCT32N, 74xx-eu:DIL14
- added IC62: 74HCT08N, 74xx-eu:DIL14
- IC40: value 74HCT32N -> 74HCT08N
- moved IC131 65.6 mm to (8.57, 41.3)
- moved IC6 49.6 mm to (3.17, 44.8)
- moved IC130 49.3 mm to (18.4, 34.3)
- moved IC89 48.0 mm to (25.4, 2.22)
- moved IC25 45.1 mm to (31.4, 9.21)
- moved IC105 42.5 mm to (30.8, 2.22)
- moved IC11 41.3 mm to (29.5, 34.3)
- moved IC57 40.5 mm to (3.49, 9.21)
- moved IC58 40.5 mm to (9.21, 9.21)
- moved IC112 39.2 mm to (30.5, 44.8)
- moved IC8 38.3 mm to (8.26, 37.8)
- moved IC60 37.6 mm to (15.2, 9.21)
- moved IC12 37.3 mm to (35.2, 34.3)
- moved IC126 36.6 mm to (29.5, 12.7)
- moved IC21 35.7 mm to (46.7, 34.3)
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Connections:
- net REG_TO_DBUS_ENABLE/CLR_NOT_CS/CLR_NOT_WE_PUSH renamed CLR_NOT_CS/CLR_NOT_WE_PUSH
- net REG_TO_DBUS_ENABLE/FILL_REGISTER_MOV renamed FILL_REGISTER_MOV
- net REG_TO_DBUS_ENABLE/PC_HIGH_LOAD_INPUT_JMP renamed PC_HIGH_LOAD_INPUT_JMP
- removed net CLR_NOT_OE/CLR_NOT_CS_CYCL_1: IC19.11, IC53.5, IC55.5, IC68.1, IC89.12, IC89.9, JP4.26
- removed net CLR_NOT_OE/CLR_NOT_CS_CYCL_2: IC49.1, IC53.9, IC55.4, IC68.5, JP4.28
- removed net IR_LOAD_INPUT/PC_COUNT_UP/!CYCL_2: IC41.11, IC49.5, IC53.8
- removed net N$108: IC103.4, IC98.7
- removed net N$114: IC103.7, IC98.9
- removed net N$116: IC103.8, IC98.12
- removed net N$121: IC61.12, IC61.8
- removed net N$124: IC103.13, IC104.4
- removed net N$125: IC103.14, IC104.7
- removed net N$126: IC19.5, IC68.3
- removed net N$127: IC103.17, IC104.9
- removed net N$134: IC103.18, IC104.12
- removed net N$139: IC88.13, IC88.5, IC88.8
- removed net N$150: IC61.10, IC61.6
- removed net N$154: IC61.3, IC61.9
- removed net N$159: IC109.11, IC40.10, IC40.13
- removed net N$17: IC103.3, IC98.4
- removed net N$200: IC19.6, IC68.6
- removed net N$252: IC61.13, IC65.6
- removed net N$266: IC129.5, IC59.13, IC59.2, IC61.11
- removed net N$32: IC55.13, IC55.8
- removed net N$33: IC55.12, IC55.6
- removed net N$79: IC112.12, IC112.8
- removed net N$90: IC65.4, IC71.3
- removed net N$91: IC1.4, IC1.8
- removed net N$96: IC103.11, IC84.11
- removed net OPCODE_LOAD_INPUT/PC_COUNT_UP/!CYCL_1: IC45.11, IC49.4, IC53.6
- removed net PTR_TO_ABUS/!PC_TO_ABUS: IC13.1, IC21.1, IC27.1, IC34.1, IC40.3
- removed net REG_TO_DBUS_B_ALU_PTR_ADD: IC84.13, IC84.3
- removed net REG_TO_DBUS_ENABLE/FILL_LR_H_SAVE_LR: IC125.6, IC44.11
- removed net REG_TO_DBUS_ENABLE/FILL_LR_L_SAVE_LR: IC44.8, IC92.6
- removed net REG_TO_DBUS_ENABLE/FILL_PC_H_RET: IC126.8, IC56.4
- removed net REG_TO_DBUS_ENABLE/FILL_PC_L_RET: IC100.3, IC56.10
- removed net REG_TO_DBUS_ENABLE/FILL_PTR_H_SET_PTR: IC125.11, IC39.6
- removed net REG_TO_DBUS_ENABLE/FILL_PTR_L_SET_PTR: IC39.3, IC92.3
- removed net REG_TO_DBUS_ENABLE/LATCH_ALU_INPUT_B/WRITE_REGB_TO_DBUS_ALU: IC1.10, IC72.3, IC84.1
- removed net REG_TO_DBUS_ENABLE/LATCH_ALU_INPUT_B/WRITE_REGB_TO_DBUS_PTR_ADD: IC84.2, IC89.3
- removed net REG_TO_DBUS_ENABLE/PC_LOW_LOAD_INPUT_JMP: IC56.9, IC72.8
- removed net REG_TO_DBUS_ENABLE/STORE_ALU_OUTPUT/STORE_CARRY_ALU: IC112.9, IC129.1, IC52.3
- removed net REG_TO_DBUS_ENABLE/STORE_ALU_OUTPUT/STORE_CARRY_TMP_JMP_O: IC112.10, IC39.11, IC78.11
- removed net REG_TO_DBUS_ENABLE/STORE_ALU_OUTPUT/STORE_CARRY_TMP_PTR_ADD: IC112.13, IC125.3, IC39.12
- removed net REG_TO_DBUS_ENABLE/WRITE_PTR_TO_ABUS/CLR_NOT_WE/CLR_NOT_CS_STR: IC130.8, IC40.2, IC67.3, IC68.2
- removed net SP_COUNT_UP: IC67.8, IC93.5
- removed net WRITE_LR_H_DBUS_RET: IC126.3, IC40.4, IC65.2
- removed net WRITE_PC_H_DBUS_SAVE_LR: IC126.11, IC65.13
- removed net WRITE_PC_L_ALU_LATCH_JMP_O: IC104.1, IC108.6, IC71.4, IC72.13, IC76.13, IC78.13, IC98.1
- removed net WRITE_REGB_TO_DBUS_SET_PTR: IC1.13, IC125.8
- removed net WRITE_REG_TO_DBUS_ALU: IC61.2, IC76.6
- removed net WRITE_REG_TO_DBUS_JMP: IC61.1, IC76.8
- removed net WRITE_REG_TO_DBUS_MOV: IC61.5, IC76.3
- removed net WRITE_REG_TO_DBUS_SELECTOR2_PUSH: IC130.6, IC17.10, IC67.9
- removed net WRITE_REG_TO_DBUS_SET_PTR: IC61.4, IC99.11
- new net CARRY&&!IR_DATA: IC62.3, IC62.4, IC88.12
- new net CARRY&&IR_DATA: IC62.12, IC62.8, IC88.4
- new net CLR_NOT_OE/CLR_NOT_CS/PC_COUNT_UP_CYCL_2: IC49.1, IC53.9, IC55.4, JP4.28
- new net CLR_NOT_OE/PC_COUNT_UP/CLR_NOT_CS_CYCL_1: IC53.5, IC55.5, IC89.12, IC89.9, JP4.26
- new net CYCLE1/CYLCE2: IC19.6, IC39.11, IC55.6, IC71.1
- new net FILL_LR_H_SAVE_LR: IC126.11, IC44.11
- new net FILL_LR_L/WRITE_PC_H_DBUS_SAVE_LR: IC44.8, IC65.13, IC92.6
- new net FILL_PC_H_RET: IC126.3, IC56.4
- new net FILL_PC_L/WRITE_LR_H_DBUS_RET: IC100.3, IC49.4, IC56.10, IC65.2
- new net FILL_PTR_H_SET_PTR: IC39.6, IC88.8
- new net FILL_PTR_L/WRITE_REGB_TO_DBUS_SET_PTR: IC1.13, IC39.3, IC92.3
- new net IR_LOAD_INPUT/!CYCL_2: IC41.11, IC53.8
- new net LATCH_ALU_INPUT_ALU/JMP_O/PTR_ADD: IC1.4, IC1.8, IC103.11
- new net LATCH_ALU_INPUT_B/WRITE_REGB_TO_DBUS_ALU: IC1.1, IC72.3
- new net LATCH_ALU_INPUT_B/WRITE_REGB_TO_DBUS_PTR_ADD: IC1.10, IC89.3
- new net MEM_OE: IC55.12, IC67.13, IC71.3
- new net OPCODE_LOAD_INPUT/!CYCL_1: IC45.11, IC53.6
- new net PC_COUNT_UP_RET: IC126.8, IC39.12
- new net PC_LOW_LOAD_INPUT_JMP: IC52.6, IC56.9
- new net PC_L_TO_DBUS: IC49.5, IC56.3, IC65.12
- new net PTR_TO_ABUS: IC13.1, IC19.5, IC21.1, IC27.1, IC34.1, IC68.3
- new net SP_COUNT_UP/WRITE_REG_TO_DBUS_SELECTOR2_PUSH: IC130.6, IC17.10, IC93.5
- new net STORE_ALU_OUTPUT/STORE_CARRY_ALU: IC112.12, IC129.1, IC72.8
- new net STORE_ALU_OUTPUT/STORE_CARRY_TMP_JMP_O: IC112.9, IC40.11
- new net STORE_ALU_OUTPUT/STORE_CARRY_TMP_PTR_ADD: IC112.10, IC52.3
- new net STORE_ALU_OUTPUT_JMP_PTR_ADD: IC112.13, IC112.8, IC67.11
- new net WQWJKDHSAAASDFXGHCJFDSAAS: IC108.6, IC40.10, IC40.13, IC40.2, IC40.5, IC71.4
- new net WRITE_PC_L_DBUS_JMP_O: IC40.8, IC56.2
- new net WRITE_PTR_TO_ABUS/CLR_NOT_WE/CLR_NOT_CS_STR: IC130.8, IC67.3, IC68.2
- net !ENABLE_REG_OUTPUT: now also IC65.5; no longer IC84.5
- net !IR_DATA_OUT_7: now also IC62.2; no longer IC40.12, IC88.12
- net ALU_CARRY_BIT: now also IC78.12; no longer IC78.9
- net ALU_OUTPUT_ENABLE/FILL_PC_L_JMP_O: now also IC40.3, IC88.13, IC88.5; no longer IC72.11, IC88.10
- net ALU_OUTPUT_ENABLE/FILL_PTR_L_PTR_ADD: now also IC62.13, IC62.5; no longer IC1.1, IC109.13
- net CARRY_LAST_CYCLE: now also IC62.1, IC62.10; no longer IC109.12, IC88.9
- net DATA0: now also IC103.3; no longer IC98.2
- net DATA1: now also IC103.4; no longer IC98.5
- net DATA2: now also IC103.7; no longer IC98.11
- net DATA3: now also IC103.8; no longer IC98.14
- net DATA4: now also IC103.13; no longer IC104.2
- net DATA5: now also IC103.14; no longer IC104.5
- net DATA6: now also IC103.17; no longer IC104.11
- net DATA7: now also IC103.18; no longer IC104.14
- net DBUS_SELECTOR_TABLE_2: no longer IC56.1
- net ENABLE_ALU_OUTPUT: now also IC55.13; no longer IC55.10
- net ENABLE_ALU_OUTPUT/FILL_REGISTER_ALU: now also IC72.11; no longer IC52.6
- net GND: now also IC62.7; no longer IC104.15, IC104.8, IC109.7, IC125.7, IC61.7, IC76.7, IC84.7, IC98.15, IC98.8
- net INPUT_REG0/OPC4/5_IS_NULL: now also IC99.13; no longer IC109.5
- net IR_DATA_OUT_7: now also IC62.9; no longer IC40.9, IC88.4
- net LATCH_ALU_INPUT_B/WRITE_REGB_TO_DBUS_JMP_O: now also IC40.6; no longer IC76.11, IC84.12
- net MEM_NOT_OE: now also IC67.12; no longer IC19.13
- net N$13: now also IC68.6; no longer IC84.8
- net N$14: now also IC67.10; no longer IC39.13
- net N$15: now also IC52.5; no longer IC72.10, IC76.10
- net N$171: now also IC49.6; no longer IC40.6
- net N$194: now also IC78.10; no longer IC125.5, IC99.10
- net N$198: now also IC78.11; no longer IC78.8
- net N$199: now also IC78.13; no longer IC78.10
- net N$2: now also IC67.9, IC99.11; no longer IC56.3, IC71.1
- net N$203: now also IC67.8; no longer IC109.6
- net N$21: now also IC68.5, IC99.12; no longer IC109.4, IC84.10
- net N$55: no longer IC76.2
- net N$80: now also IC68.4; no longer IC84.9
- net N$85: now also IC65.4; no longer IC84.4
- net N$97: now also IC88.10; no longer IC125.10, IC125.13, IC99.13
- net OPERAND_REGB_OUTPUT: no longer IC56.2
- net PC_COUNT_UP: now also IC39.13; no longer IC49.6
- net PC_DATA_OUT_0: no longer IC98.3
- net PC_DATA_OUT_1: no longer IC98.6
- net PC_DATA_OUT_2: no longer IC98.10
- net PC_DATA_OUT_3: no longer IC98.13
- net PC_DATA_OUT_4: no longer IC104.3
- net PC_DATA_OUT_5: no longer IC104.6
- net PC_DATA_OUT_6: no longer IC104.10
- net PC_DATA_OUT_7: no longer IC104.13
- net POP: now also IC130.13; no longer IC109.2
- net PTR_ADD: now also IC52.2; no longer IC125.2
- net PTR_HIGH_COUNT_DOWN: now also IC62.11; no longer IC40.8
- net PTR_HIGH_COUNT_UP: now also IC62.6; no longer IC40.11
- net REGS_OUTPUT_TO_DATABUS_ENABLE: now also IC65.6; no longer IC84.6
- net RING_CNTR_CLOCK: now also IC129.5, IC59.13, IC59.2
- net SECOND_LATCH_SELECT: no longer IC65.5
- net SELECT_CARRY_BIT: now also IC72.10, IC72.13; no longer IC52.2, IC52.5, IC76.5
- net SP_COUNT_DOWN: now also IC130.11; no longer IC109.3
- net STATE_0/CYCL_3: now also IC40.9, IC78.9; no longer IC76.1, IC76.12, IC76.4, IC76.9, IC99.12, IC99.9
- net STATE_1/CYCL_4: now also IC130.12, IC40.4, IC52.4; no longer IC109.1, IC72.9, IC78.12
- net STATE_2/CYCL_5: now also IC40.12, IC72.9, IC88.9; no longer IC125.1, IC125.9, IC72.12
- net STATE_3/CYCL_6: now also IC40.1, IC72.12; no longer IC125.12, IC125.4, IC52.4
- net VCC: now also IC62.14; no longer IC104.16, IC109.14, IC125.14, IC61.14, IC76.14, IC84.14, IC98.16
- net WRITE_PC_L_DBUS_SAVE_LR: now also IC56.1, IC78.8; no longer IC40.5, IC65.12, IC99.8
- net WRITE_PTR_L_TO_DBUS_PTR_ADD: no longer IC71.2
- net WRITE_PTR_TO_ABUS/CLR_NOT_OE/CLR_NOT_CS/FILL_REGISTER_LDR: now also IC68.1, IC71.2; no longer IC19.12, IC40.1, IC55.9, IC68.4
